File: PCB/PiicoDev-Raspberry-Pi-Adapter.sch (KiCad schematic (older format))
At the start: 12 parts, among them J1 Raspberry_Pi_2_3, J2 Conn_PiicoDev_socket, J3 Conn_PiicoDev_socket, J4 Conn_PiicoDev_socket, J5 Conn_PiicoDev_socket, J6 Prototyping Header

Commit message: Add Logo to silkscreen
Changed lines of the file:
@@
 L CoreElectronics_Artwork:LOGO_CoreElectronics_made-with-love G2
 U 1 1 602FAEEA
-P 9950 6300
-F 0 "G2" H 9950 6094 60  0001 C CNN
-F 1 "LOGO_CoreElectronics_made-with-love" H 9950 6506 60  0001 C CNN
-F 2 "CoreElectronics_Artwork:piicodev_logo_10.2x2.5mm" H 9950 6300 50  0001 C CNN
-F 3 "" H 9950 6300 50  0001 C CNN
-	1    9950 6300
+P 10350 6300
+F 0 "G2" H 10350 6094 60  0001 C CNN
+F 1 "LOGO_CoreElectronics_made-with-love" H 10350 6506 60  0001 C CNN
+F 2 "CoreElectronics_Artwork:piicodev_logo_10.2x2.5mm" H 10350 6300 50  0001 C CNN
+F 3 "" H 10350 6300 50  0001 C CNN
+	1    10350 6300
 	1    0    0    -1
 $EndComp

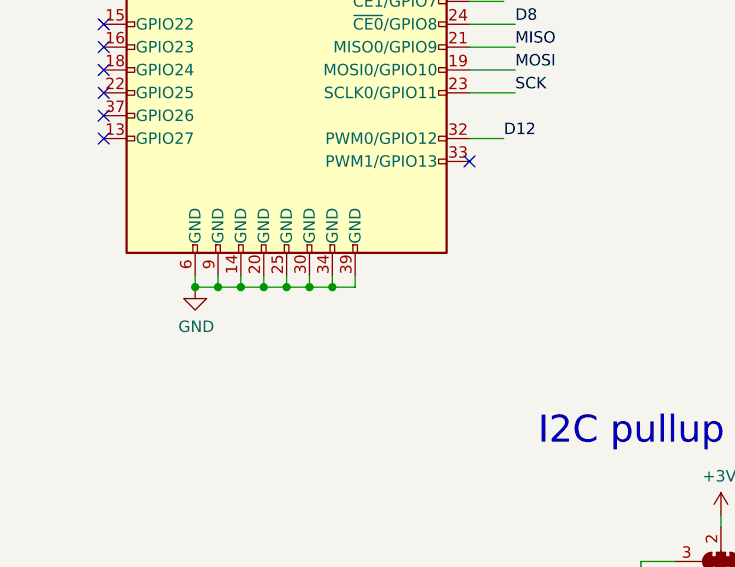
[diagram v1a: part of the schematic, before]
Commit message: Bump to v11 - update header footprint to include post-holes
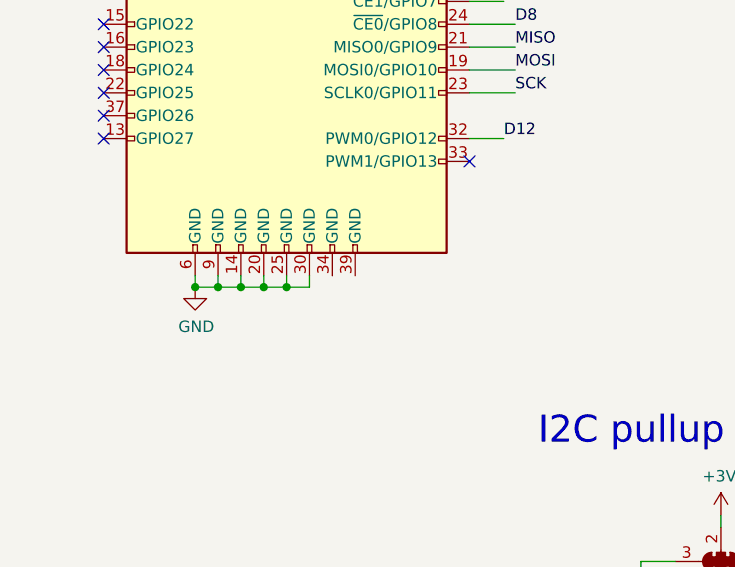
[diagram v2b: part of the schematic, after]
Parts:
- G1: footprint CoreElectronics_Artwork:piicodev_logo_v2_14.2x3.2mm -> CoreElectronics_Artwork:piicodev_logo_10.2x2.5mm
- J1: footprint Connector_PinSocket_2.54mm:PinSocket_2x20_P2.54mm_Vertical_SMD -> CoreElectronics_Components:PinSocket_2x20_P2.54mm_Vertical_SMD_With_Post
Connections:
- net GND: no longer J1.34 (GND), J1.39 (GND)
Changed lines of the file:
@@
 Sheet 1 1
 Title "PiicoDev Adapter for Raspberry Pi"
-Date "2021-03-31"
-Rev "v10"
+Date "2021-06-28"
+Rev "v11"
 Comp "Core Electronics"
 Comment1 "Based off the design by SparkFun: https://github.com/sparkfun/Qwiic_Hat_for_Raspberry_Pi"
@@
 F 0 "J1" H 2550 5381 50  0000 C CNN
 F 1 "Raspberry_Pi_2_3" H 2550 5290 50  0000 C CNN
-F 2 "Connector_PinSocket_2.54mm:PinSocket_2x20_P2.54mm_Vertical_SMD" H 2550 3900 50  0001 C CNN
+F 2 "CoreElectronics_Components:PinSocket_2x20_P2.54mm_Vertical_SMD_With_Post" H 2550 3900 50  0001 C CNN
 F 3 "https://www.raspberrypi.org/documentation/hardware/raspberrypi/schematics/rpi_SCH_3bplus_1p0_reduced.pdf" H 2550 3900 50  0001 C CNN
 	1    2550 3900
@@
 F 0 "G1" H 8000 6095 60  0001 C CNN
 F 1 "LOGO_PiicoDev" H 8000 6505 60  0001 C CNN
-F 2 "CoreElectronics_Artwork:piicodev_logo_v2_14.2x3.2mm" H 8000 6300 50  0001 C CNN
+F 2 "CoreElectronics_Artwork:piicodev_logo_10.2x2.5mm" H 8000 6300 50  0001 C CNN
 F 3 "" H 8000 6300 50  0001 C CNN
 	1    8000 6300
@@
 	2650 5250 2650 5200
 Connection ~ 2550 5250
-Wire Wire Line
-	2650 5250 2750 5250
-Wire Wire Line
-	2750 5250 2750 5200
-Connection ~ 2650 5250
-Wire Wire Line
-	2750 5250 2850 5250
-Wire Wire Line
-	2850 5250 2850 5200
-Connection ~ 2750 5250
 NoConn ~ 3350 3000
 NoConn ~ 3350 3100

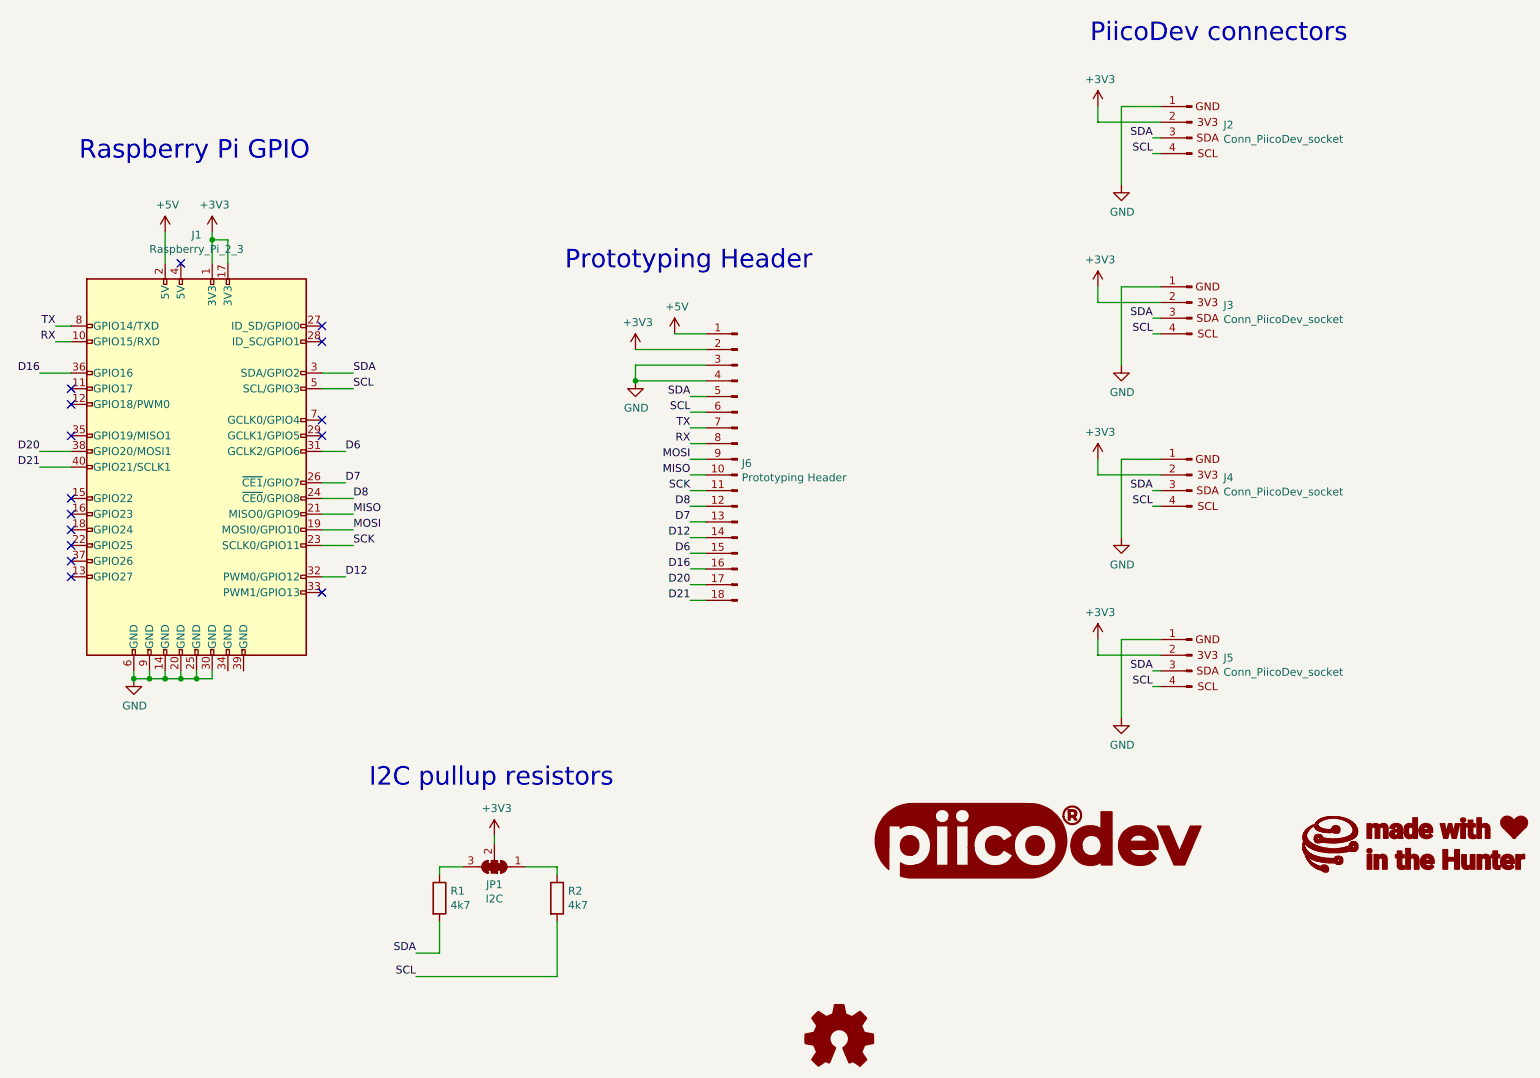
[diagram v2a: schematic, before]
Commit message: Add 120R to SCL & SDA.  Improve silk screen.
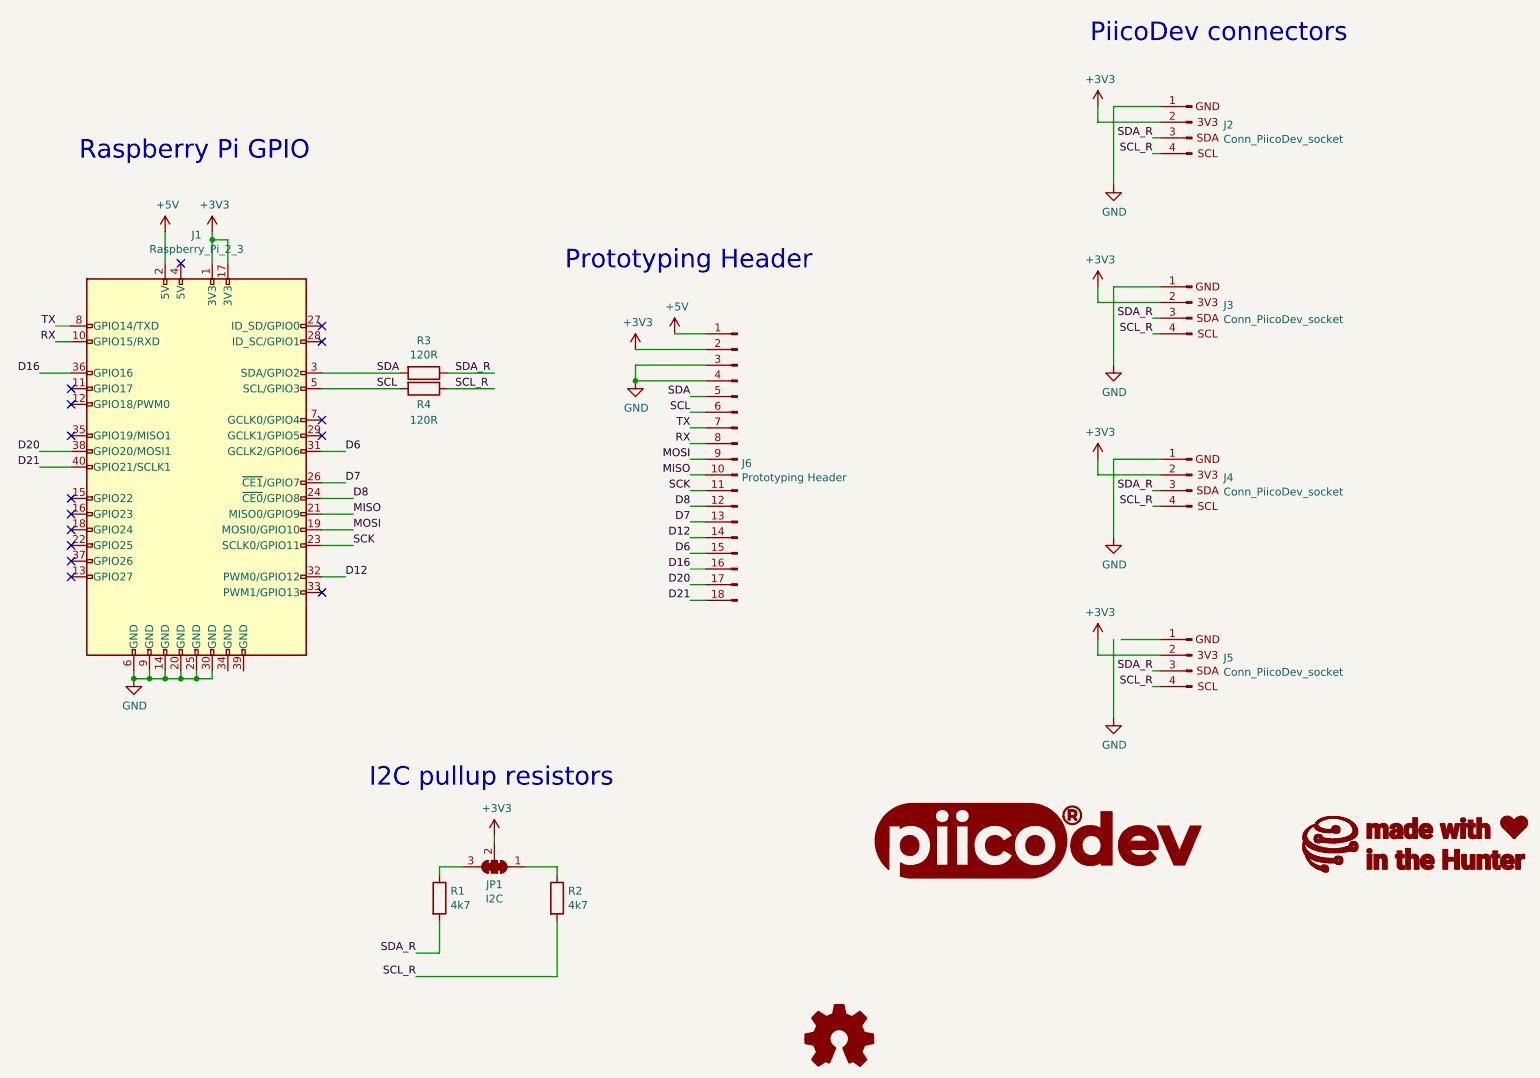
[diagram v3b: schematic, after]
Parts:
- added R3, R4: 120R, Resistor_SMD:R_0402_1005Metric, symbol Device:R
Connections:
- net labels added: SCL_R, SDA_R
- wire segments 82 -> 84
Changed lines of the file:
@@
 Sheet 1 1
 Title "PiicoDev Adapter for Raspberry Pi"
-Date "2021-06-28"
-Rev "v11"
+Date "2021-10-29"
+Rev "v12"
 Comp "Core Electronics"
 Comment1 "Based off the design by SparkFun: https://github.com/sparkfun/Qwiic_Hat_for_Raspberry_Pi"
@@
 $EndDescr
 $Comp
-L power:+3V3 #PWR?
+L power:+3V3 #PWR08
 U 1 1 602A11D2
 P 8300 1600
-F 0 "#PWR?" H 8300 1450 50  0001 C CNN
+F 0 "#PWR08" H 8300 1450 50  0001 C CNN
 F 1 "+3V3" H 8315 1773 50  0000 C CNN
 F 2 "" H 8300 1600 50  0001 C CNN
@@
 $EndComp
 $Comp
-L power:GND #PWR?
+L power:GND #PWR012
 U 1 1 602A1DA4
-P 8450 2100
-F 0 "#PWR?" H 8450 1850 50  0001 C CNN
-F 1 "GND" H 8455 1927 50  0000 C CNN
-F 2 "" H 8450 2100 50  0001 C CNN
-F 3 "" H 8450 2100 50  0001 C CNN
-	1    8450 2100
-	1    0    0    -1
-$EndComp
-Wire Wire Line
-	8700 1600 8450 1600
-Wire Wire Line
-	8450 1600 8450 2100
+P 8400 2100
+F 0 "#PWR012" H 8400 1850 50  0001 C CNN
+F 1 "GND" H 8405 1927 50  0000 C CNN
+F 2 "" H 8400 2100 50  0001 C CNN
+F 3 "" H 8400 2100 50  0001 C CNN
+	1    8400 2100
+	1    0    0    -1
+$EndComp
+Wire Wire Line
+	8400 1600 8400 2100
 Wire Wire Line
 	8300 1600 8300 1700
@@
 	8300 1700 8700 1700
 Text Label 8650 1800 2    50   ~ 0
-SDA
+SDA_R
 Text Label 8650 1900 2    50   ~ 0
-SCL
+SCL_R
 Wire Wire Line
 	8650 1900 8700 1900
@@
 	8650 1800 8700 1800
 $Comp
-L power:+3V3 #PWR?
+L power:+3V3 #PWR09
 U 1 1 602A7B49
 P 8300 2750
-F 0 "#PWR?" H 8300 2600 50  0001 C CNN
+F 0 "#PWR09" H 8300 2600 50  0001 C CNN
 F 1 "+3V3" H 8315 2923 50  0000 C CNN
 F 2 "" H 8300 2750 50  0001 C CNN
@@
 $EndComp
 $Comp
-L power:GND #PWR?
+L power:GND #PWR013
 U 1 1 602A7B4F
-P 8450 3250
-F 0 "#PWR?" H 8450 3000 50  0001 C CNN
-F 1 "GND" H 8455 3077 50  0000 C CNN
-F 2 "" H 8450 3250 50  0001 C CNN
-F 3 "" H 8450 3250 50  0001 C CNN
-	1    8450 3250
-	1    0    0    -1
-$EndComp
-Wire Wire Line
-	8700 2750 8450 2750
-Wire Wire Line
-	8450 2750 8450 3250
+P 8400 3250
+F 0 "#PWR013" H 8400 3000 50  0001 C CNN
+F 1 "GND" H 8405 3077 50  0000 C CNN
+F 2 "" H 8400 3250 50  0001 C CNN
+F 3 "" H 8400 3250 50  0001 C CNN
+	1    8400 3250
+	1    0    0    -1
+$EndComp
+Wire Wire Line
+	8400 2750 8400 3250
 Wire Wire Line
 	8300 2750 8300 2850
@@
 	8300 2850 8700 2850
 Text Label 8650 2950 2    50   ~ 0
-SDA
+SDA_R
 Text Label 8650 3050 2    50   ~ 0
-SCL
+SCL_R
 Wire Wire Line
 	8650 3050 8700 3050
@@
 	8650 2950 8700 2950
 $Comp
-L power:+3V3 #PWR?
+L power:+3V3 #PWR010
 U 1 1 602A891A
 P 8300 3850
-F 0 "#PWR?" H 8300 3700 50  0001 C CNN
+F 0 "#PWR010" H 8300 3700 50  0001 C CNN
 F 1 "+3V3" H 8315 4023 50  0000 C CNN
 F 2 "" H 8300 3850 50  0001 C CNN
@@
 $EndComp
 $Comp
-L power:GND #PWR?
+L power:GND #PWR014
 U 1 1 602A8920
-P 8450 4350
-F 0 "#PWR?" H 8450 4100 50  0001 C CNN
-F 1 "GND" H 8455 4177 50  0000 C CNN
-F 2 "" H 8450 4350 50  0001 C CNN
-F 3 "" H 8450 4350 50  0001 C CNN
-	1    8450 4350
-	1    0    0    -1
-$EndComp
-Wire Wire Line
-	8700 3850 8450 3850
-Wire Wire Line
-	8450 3850 8450 4350
+P 8400 4350
+F 0 "#PWR014" H 8400 4100 50  0001 C CNN
+F 1 "GND" H 8405 4177 50  0000 C CNN
+F 2 "" H 8400 4350 50  0001 C CNN
+F 3 "" H 8400 4350 50  0001 C CNN
+	1    8400 4350
+	1    0    0    -1
+$EndComp
+Wire Wire Line
+	8400 3850 8400 4350
 Wire Wire Line
 	8300 3850 8300 3950
@@
 	8300 3950 8700 3950
 Text Label 8650 4050 2    50   ~ 0
-SDA
+SDA_R
 Text Label 8650 4150 2    50   ~ 0
-SCL
+SCL_R
 Wire Wire Line
 	8650 4150 8700 4150
@@
 	8650 4050 8700 4050
 $Comp
-L power:+3V3 #PWR?
+L power:+3V3 #PWR011
 U 1 1 602AA2FA
 P 8300 5000
-F 0 "#PWR?" H 8300 4850 50  0001 C CNN
+F 0 "#PWR011" H 8300 4850 50  0001 C CNN
 F 1 "+3V3" H 8315 5173 50  0000 C CNN
 F 2 "" H 8300 5000 50  0001 C CNN
@@
 $EndComp
 $Comp
-L power:GND #PWR?
+L power:GND #PWR015
 U 1 1 602AA300
-P 8450 5500
-F 0 "#PWR?" H 8450 5250 50  0001 C CNN
-F 1 "GND" H 8455 5327 50  0000 C CNN
-F 2 "" H 8450 5500 50  0001 C CNN
-F 3 "" H 8450 5500 50  0001 C CNN
-	1    8450 5500
+P 8400 5500
+F 0 "#PWR015" H 8400 5250 50  0001 C CNN
+F 1 "GND" H 8405 5327 50  0000 C CNN
+F 2 "" H 8400 5500 50  0001 C CNN
+F 3 "" H 8400 5500 50  0001 C CNN
+	1    8400 5500
 	1    0    0    -1
 $EndComp
@@
 	8700 5000 8450 5000
 Wire Wire Line
-	8450 5000 8450 5500
+	8400 5000 8400 5500
 Wire Wire Line
 	8300 5000 8300 5100
@@
 	8300 5100 8700 5100
 Text Label 8650 5200 2    50   ~ 0
-SDA
+SDA_R
 Text Label 8650 5300 2    50   ~ 0
-SCL
+SCL_R
 Wire Wire Line
 	8650 5300 8700 5300
@@
 $EndComp
 $Comp
-L power:GND #PWR?
+L power:GND #PWR01
 U 1 1 602B532C
 P 2150 5250
-F 0 "#PWR?" H 2150 5000 50  0001 C CNN
+F 0 "#PWR01" H 2150 5000 50  0001 C CNN
 F 1 "GND" H 2155 5077 50  0000 C CNN
 F 2 "" H 2150 5250 50  0001 C CNN
@@
 Wire Wire Line
 	2150 5250 2150 5200
-Text Label 3550 3300 0    50   ~ 0
+Text Label 3700 3300 0    50   ~ 0
 SDA
-Wire Wire Line
-	3550 3300 3350 3300
-Text Label 3550 3400 0    50   ~ 0
+Text Label 3700 3400 0    50   ~ 0
 SCL
-Wire Wire Line
-	3550 3400 3350 3400
-$Comp
-L power:+3V3 #PWR?
+$Comp
+L power:+3V3 #PWR03
 U 1 1 602B762E
 P 2650 2400
-F 0 "#PWR?" H 2650 2250 50  0001 C CNN
+F 0 "#PWR03" H 2650 2250 50  0001 C CNN
 F 1 "+3V3" H 2665 2573 50  0000 C CNN
 F 2 "" H 2650 2400 50  0001 C CNN
@@
 $EndComp
 $Comp
-L power:+3V3 #PWR?
+L power:+3V3 #PWR05
 U 1 1 602C7AEC
 P 5350 3150
-F 0 "#PWR?" H 5350 3000 50  0001 C CNN
+F 0 "#PWR05" H 5350 3000 50  0001 C CNN
 F 1 "+3V3" H 5365 3323 50  0000 C CNN
 F 2 "" H 5350 3150 50  0001 C CNN
@@
 	5350 3150 5800 3150
 $Comp
-L power:+5V #PWR?
+L power:+5V #PWR02
 U 1 1 602C8A49
 P 2350 2400
-F 0 "#PWR?" H 2350 2250 50  0001 C CNN
+F 0 "#PWR02" H 2350 2250 50  0001 C CNN
 F 1 "+5V" H 2365 2573 50  0000 C CNN
 F 2 "" H 2350 2400 50  0001 C CNN
@@
 	2650 2450 2650 2400
 $Comp
-L power:+5V #PWR?
+L power:+5V #PWR07
 U 1 1 602CAD3B
 P 5600 3050
-F 0 "#PWR?" H 5600 2900 50  0001 C CNN
+F 0 "#PWR07" H 5600 2900 50  0001 C CNN
 F 1 "+5V" H 5615 3223 50  0000 C CNN
 F 2 "" H 5600 3050 50  0001 C CNN
@@
 	5600 3050 5800 3050
 $Comp
-L power:GND #PWR?
+L power:GND #PWR06
 U 1 1 602CC0E8
 P 5350 3350
-F 0 "#PWR?" H 5350 3100 50  0001 C CNN
+F 0 "#PWR06" H 5350 3100 50  0001 C CNN
 F 1 "GND" H 5355 3177 50  0000 C CNN
 F 2 "" H 5350 3350 50  0001 C CNN
@@
 NoConn ~ 2450 2600
 Text Label 3950 7000 2    50   ~ 0
-SDA
+SDA_R
 Text Label 3950 7150 2    50   ~ 0
-SCL
+SCL_R
 $Comp
 L Jumper:SolderJumper_3_Bridged123 JP1
@@
 $EndComp
 $Comp
-L power:+3V3 #PWR?
+L power:+3V3 #PWR04
 U 1 1 6045CC2C
 P 4450 6250
-F 0 "#PWR?" H 4450 6100 50  0001 C CNN
+F 0 "#PWR04" H 4450 6100 50  0001 C CNN
 F 1 "+3V3" H 4465 6423 50  0000 C CNN
 F 2 "" H 4450 6250 50  0001 C CNN
@@
 Text Notes 3650 5950 0    118  ~ 0
 I2C pullup resistors
+$Comp
+L Device:R R3
+U 1 1 617A5DE3
+P 4000 3300
+F 0 "R3" V 3793 3300 50  0000 C CNN
+F 1 "120R" V 3884 3300 50  0000 C CNN
+F 2 "Resistor_SMD:R_0402_1005Metric" V 3930 3300 50  0001 C CNN
+F 3 "~" H 4000 3300 50  0001 C CNN
+	1    4000 3300
+	0    1    1    0
+$EndComp
+$Comp
+L Device:R R4
+U 1 1 617A67C8
+P 4000 3400
+F 0 "R4" V 4100 3400 50  0000 C CNN
+F 1 "120R" V 4200 3400 50  0000 C CNN
+F 2 "Resistor_SMD:R_0402_1005Metric" V 3930 3400 50  0001 C CNN
+F 3 "~" H 4000 3400 50  0001 C CNN
+	1    4000 3400
+	0    1    1    0
+$EndComp
+Wire Wire Line
+	3350 3300 3850 3300
+Wire Wire Line
+	3350 3400 3850 3400
+Text Label 4200 3300 0    50   ~ 0
+SDA_R
+Wire Wire Line
+	4150 3300 4450 3300
+Wire Wire Line
+	4150 3400 4450 3400
+Text Label 4200 3400 0    50   ~ 0
+SCL_R
+Wire Wire Line
+	8400 1600 8700 1600
+Wire Wire Line
+	8400 2750 8700 2750
+Wire Wire Line
+	8400 3850 8700 3850
 $EndSCHEMATC
